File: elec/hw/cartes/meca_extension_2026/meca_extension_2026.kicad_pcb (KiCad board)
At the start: 2 copper layers, 126.2 x 84.5 mm, 177 parts, among them J1 2-1445051-3, J10 22053051, J11 B2B-XH-A, J12 22272021, J13 22053051, J14 22272031, J15 22272031, J16 5264-3P, J17 5267-3P, J18 5267-3P, J19 5267-3P, J2 B2B-XH-A, J20 5267-3P, J24 22053031, J25 22053031, J26 22053051, J27 22053041, J28 22053031, J29 22053031, J3 22272021, J4 22053051, J5 B2B-XH-A, J6 22272021, J7 22053051, J8 B2B-XH-A, J9 22272021, Q1 SI2310, Q10 SI2310, Q11 SI2310, Q12 2N7002, Q19 BSS84, Q2 SI2310, Q20 2N7002, Q3 2N7002, Q4 SI2310, Q5 SI2310, Q6 2N7002, Q7 SI2310, Q8 SI2310, Q9 2N7002, U1 TCA9548APWR, U11 LV14340DDAR, U2 PCA9535PW, U3 TLA2528IRTER, U4 TLV9061IDBVR, U5 TLV9061IDBVR, U6 TLV9061IDBVR, U7 TLV9061IDBVR, U8 74HCT238PW

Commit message: meca_extension : led added and J1 moved
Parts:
- moved J27 4.30 mm to (129.9, 52.4), turned to 60 degrees
- moved J26 2.82 mm to (121.5, 56.5), turned to 60 degrees
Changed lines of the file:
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@@
 		(tags "capacitor")
 		(property "Reference" "D9"
-			(at 66.5 7.07 180)
+			(at 0 1.75 180)
 			(layer "F.SilkS")
 			(effects
@@
 	(footprint "cocotter_connectors:22272041"
 		(layer "B.Cu")
-		(at 130.400148 56.635 -60)
+		(at 129.900148 52.365 60)
 		(property "Reference" "J27"
-			(at 0 6.35 120)
+			(at 0 6.35 240)
 			(unlocked yes)
 			(layer "B.SilkS")
@@
 		)
 		(property "Value" "22053041"
-			(at 0 -1.06 120)
+			(at 0 -1.06 240)
 			(unlocked yes)
 			(layer "B.Fab")
@@
 		)
 		(property "Datasheet" "https://www.molex.com/en-us/products/part-detail/22272041"
-			(at -0.000001 2.540001 120)
+			(at -0.000001 2.540001 240)
 			(unlocked yes)
 			(layer "B.Fab")
@@
 		)
 		(property "Description" "mini kk 4 voies vertical"
-			(at -0.000001 2.540001 120)
+			(at -0.000001 2.540001 240)
 			(unlocked yes)
 			(layer "B.Fab")
@@
 		)
 		(property "JLCPCB Part #" "C504991"
-			(at 0 0 300)
+			(at 0 0 60)
 			(unlocked yes)
 			(layer "B.Fab")
@@
 		(attr smd)
 		(fp_line
-			(start -2.899999 5.079999)
-			(end 2.9 5.08)
+			(start 2.899999 -5.079999)
+			(end -2.9 -5.08)
 			(stroke
 				(width 0.12)
@@
 		)
 		(fp_line
-			(start -2.9 3.81)
-			(end -2.9 -1.270001)
+			(start 2.899999 -5.079999)
+			(end 2.9 5.08)
 			(stroke
 				(width 0.12)
@@
 		)
 		(fp_line
-			(start -1.9 3.810001)
-			(end -1.9 -1.27)
+			(start -2.9 3.81)
+			(end -2.9 -1.270001)
 			(stroke
 				(width 0.12)
@@
 		)
 		(fp_line
-			(start 2.899999 -5.079999)
-			(end 2.9 5.08)
+			(start -1.9 3.810001)
+			(end -1.9 -1.27)
 			(stroke
 				(width 0.12)
@@
 		)
 		(fp_line
-			(start 2.899999 -5.079999)
-			(end -2.9 -5.08)
+			(start -2.899999 5.079999)
+			(end 2.9 5.08)
 			(stroke
 				(width 0.12)
@@
 		)
 		(fp_line
-			(start -2.899999 5.079999)
-			(end 2.9 5.08)
+			(start 2.899999 -5.079999)
+			(end -2.9 -5.08)
 			(stroke
 				(width 0.1)
@@
 		)
 		(fp_line
-			(start 2.9 5.08)
-			(end 2.899999 -5.079999)
+			(start -2.9 0)
+			(end -2.899999 5.079999)
 			(stroke
 				(width 0.1)
@@
 		)
 		(fp_line
-			(start -2.9 0)
-			(end -2.899999 5.079999)
+			(start -2.899999 5.079999)
+			(end 2.9 5.08)
 			(stroke
 				(width 0.1)
@@
 		)
 		(fp_line
-			(start 2.899999 -5.079999)
-			(end -2.9 -5.08)
+			(start 2.9 5.08)
+			(end 2.899999 -5.079999)
 			(stroke
 				(width 0.1)
@@
 		)
 		(fp_text user "${REFERENCE}"
-			(at 0 -1.23 120)
+			(at 0 -1.23 240)
 			(unlocked yes)
 			(layer "B.Fab")
@@
 		)
 		(pad "1" thru_hole rect
-			(at 0.000001 3.81 300)
+			(at 0.000001 3.81 60)
 			(size 2 2)
 			(drill 1.2)
@@
 		)
 		(pad "2" thru_hole oval
-			(at 0 1.27 300)
+			(at 0 1.27 60)
 			(size 2 2)
 			(drill 1.2)
@@
 		)
 		(pad "3" thru_hole oval
-			(at 0 -1.27 300)
+			(at 0 -1.27 60)
 			(size 2 2)
 			(drill 1.2)
@@
 		)
 		(pad "4" thru_hole oval
-			(at -0.000001 -3.81 300)
+			(at -0.000001 -3.81 60)
 			(size 2 2)
 			(drill 1.2)
@@
 	(footprint "cocotter_connectors:22272051"
 		(layer "B.Cu")
-		(at 120.800295 53.770001 120)
+		(at 121.5 56.5 60)
 		(property "Reference" "J26"
-			(at 0 7.62 300)
+			(at 0 7.62 240)
 			(unlocked yes)
 			(layer "B.SilkS")
@@
 		)
 		(property "Value" "22053051"
-			(at 0 -7.62 300)
+			(at 0 -7.62 240)
 			(unlocked yes)
 			(layer "B.Fab")
@@
 		)
 		(property "Datasheet" "https://www.molex.com/en-us/products/part-detail/22272051"
-			(at -0.000001 3.81 300)
+			(at -0.000001 3.81 240)
 			(unlocked yes)
 			(layer "B.Fab")
@@
 		)
 		(property "Description" "mini kk 5 voies vertical"
-			(at -0.000001 3.81 300)
+			(at -0.000001 3.81 240)
 			(unlocked yes)
 			(layer "B.Fab")
@@
 		)
 		(property "JLCPCB Part #" "C585785"
-			(at 0 0 120)
+			(at 0 0 60)
 			(unlocked yes)
 			(layer "B.Fab")
@@
 		)
 		(fp_line
-			(start -1.900001 3.81)
-			(end -1.9 -1.27)
+			(start -2.899999 3.81)
+			(end -2.9 -1.27)
 			(stroke
 				(width 0.12)
@@
 		)
 		(fp_line
-			(start -2.899999 3.81)
-			(end -2.9 -1.27)
+			(start -1.900001 3.81)
+			(end -1.9 -1.27)
 			(stroke
 				(width 0.12)
@@
 		(fp_poly
 			(pts
-				(xy -3.400001 6.81) (xy 3.400001 6.809999) (xy 3.400001 -6.81) (xy -3.400001 -6.809999)
+				(xy -3.400001 6.809999) (xy 3.400001 6.809999) (xy 3.400001 -6.809999) (xy -3.400001 -6.809999)
 			)
 			(stroke
@@
 		)
 		(fp_line
-			(start 2.9 6.35)
-			(end 2.900001 -6.35)
+			(start -2.900001 6.35)
+			(end 2.9 6.35)
 			(stroke
 				(width 0.1)
@@
 		)
 		(fp_line
-			(start -2.900001 6.35)
-			(end 2.9 6.35)
+			(start 2.9 6.35)
+			(end 2.900001 -6.35)
 			(stroke
 				(width 0.1)
@@
 		)
 		(fp_text user "${REFERENCE}"
-			(at 0 7.62 300)
+			(at 0 7.62 240)
 			(unlocked yes)
 			(layer "B.Fab")
@@
 		)
 		(pad "1" thru_hole rect
-			(at 0 5.08 120)
+			(at 0 5.08 60)
 			(size 2 2)
 			(drill 1.2)
@@
 		)
 		(pad "2" thru_hole oval
-			(at 0.000001 2.540001 120)
+			(at 0.000001 2.540001 60)
 			(size 2 2)
 			(drill 1.2)
@@
 		)
 		(pad "3" thru_hole oval
-			(at 0 0 120)
+			(at 0 0 60)
 			(size 2 2)
 			(drill 1.2)
@@
 		)
 		(pad "4" thru_hole oval
-			(at -0.000001 -2.540001 120)
+			(at -0.000001 -2.540001 60)
 			(size 2 2)
 			(drill 1.2)
@@
 		)
 		(pad "5" thru_hole oval
-			(at 0 -5.08 120)
+			(at 0 -5.08 60)
 			(size 2 2)
 			(drill 1.2)

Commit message: meca_ext: layout almost done
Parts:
- added R58: 2k2 1%, cocotter_resistor:r0603_reflow, B.Cu at (117.0, 88.5)
- added R59: 2k2 1%, cocotter_resistor:r0603_reflow, B.Cu at (115.0, 86.5)
- added R60: 2k2 1%, cocotter_resistor:r0603_reflow, B.Cu at (127.0, 87.3)
- added R61: 2k2 1%, cocotter_resistor:r0603_reflow, B.Cu at (127.0, 89.5)
- added TP5: TestPoint, cocotter_others:testpoint-THT-0.8mm, B.Cu at (119.5, 88.5)
- added TP6: TestPoint, cocotter_others:testpoint-THT-0.8mm, B.Cu at (117.5, 86.5)
- added TP7: TestPoint, cocotter_others:testpoint-THT-0.8mm, B.Cu at (123.5, 87.5)
- added TP8: TestPoint, cocotter_others:testpoint-THT-0.8mm, B.Cu at (123.5, 89.5)
- D9: moved to B.Cu
- moved R57 43.7 mm to (98.0, 81.3)
- moved D9 41.6 mm to (101.2, 81.3), turned to 180 degrees
- moved C1 16.3 mm to (131.0, 59.0), turned to -30 degrees
- moved R76 14.1 mm to (122.5, 62.5), turned to -30 degrees
- moved C12 9.82 mm to (177.0, 113.0), turned to 105 degrees
- moved R78 7.28 mm to (98.0, 95.0), turned to 180 degrees
- moved C21 6.04 mm to (100.0, 100.5), turned to 180 degrees
- moved C9 6.02 mm to (94.0, 76.0), turned to 180 degrees
- moved R77 5.70 mm to (101.0, 95.0), turned to 180 degrees
- moved R56 4.92 mm to (145.0, 86.0), turned to 90 degrees
- moved C13 4.03 mm to (100.0, 97.5), turned to 180 degrees
- moved C10 3.04 mm to (72.0, 98.5), turned to 180 degrees
- moved R79 1.76 mm to (97.0, 93.5), turned to 180 degrees
- moved C2 1.67 mm to (147.5, 96.8), turned to 90 degrees
- moved R46 1.41 mm to (95.5, 69.5), turned to 180 degrees
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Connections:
- J27 pad 1: /scl_3v3 -> GND
- J27 pad 2: /sda_3v3 -> /scl_3v3
- J27 pad 3: +3.3V -> /sda_3v3
- J27 pad 4: unconnected-(J27-Pad4) -> +3.3V
- U1 pad 13: /sda_4_3v3 -> Net-(U1-SD4)
- U1 pad 14: /scl_4_3v3 -> Net-(U1-SC4)
- U1 pad 15: /sda_5_3v3 -> Net-(U1-SD5)
- U1 pad 16: /scl_5_3v3 -> Net-(U1-SC5)
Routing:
- net +BATT: track 0.00 -> 300.8 mm
- net +5V: track 0.00 -> 222.8 mm, vias 0 -> 1
- net /digital_servo_cmd_3v3: track 0.00 -> 206.1 mm
- net /color_led_cmd_3v3: track 0.00 -> 197.9 mm, vias 0 -> 5
- net +3.3V: track 0.00 -> 197.9 mm, vias 0 -> 21
- net /scl_3v3: track 0.00 -> 154.4 mm, vias 0 -> 4
- net +6V: track 0.00 -> 153.8 mm, vias 0 -> 3
- net /sda_3v3: track 0.00 -> 152.7 mm, vias 0 -> 4
- net /pmp_cmd_0_3v3: track 0.00 -> 109.6 mm, vias 0 -> 2
- net /neopixel_cmd_3v3: track 0.00 -> 107.3 mm, vias 0 -> 1
- net /solenoid_valve_cmd_0_3v3: track 0.00 -> 93.1 mm, vias 0 -> 2
- net /neopixel_cmd_3_3v3: track 0.00 -> 84.4 mm, vias 0 -> 2
- net /pump_current_3_3v3: track 0.00 -> 83.2 mm, vias 0 -> 2
- net /pmp_cmd_1_3v3: track 0.00 -> 76.4 mm, vias 0 -> 4
- net /sda_2_3v3: track 0.00 -> 76.3 mm, vias 0 -> 2
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- added copper zone on In2.Cu, net +3.3V
- added copper zone on B.Cu, net +6V
- added copper zone on B.Cu, net GND
- added copper zone on F.Cu, net GND
- added copper zone on In1.Cu, net GND
- added copper zone on In2.Cu, net GND
- added copper zone on B.Cu, net Net-(C16-Pad1)
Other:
- copper layers 2 -> 4
- board text removed: "trous de fixation a replacer correctement, je les ai juste jetés"

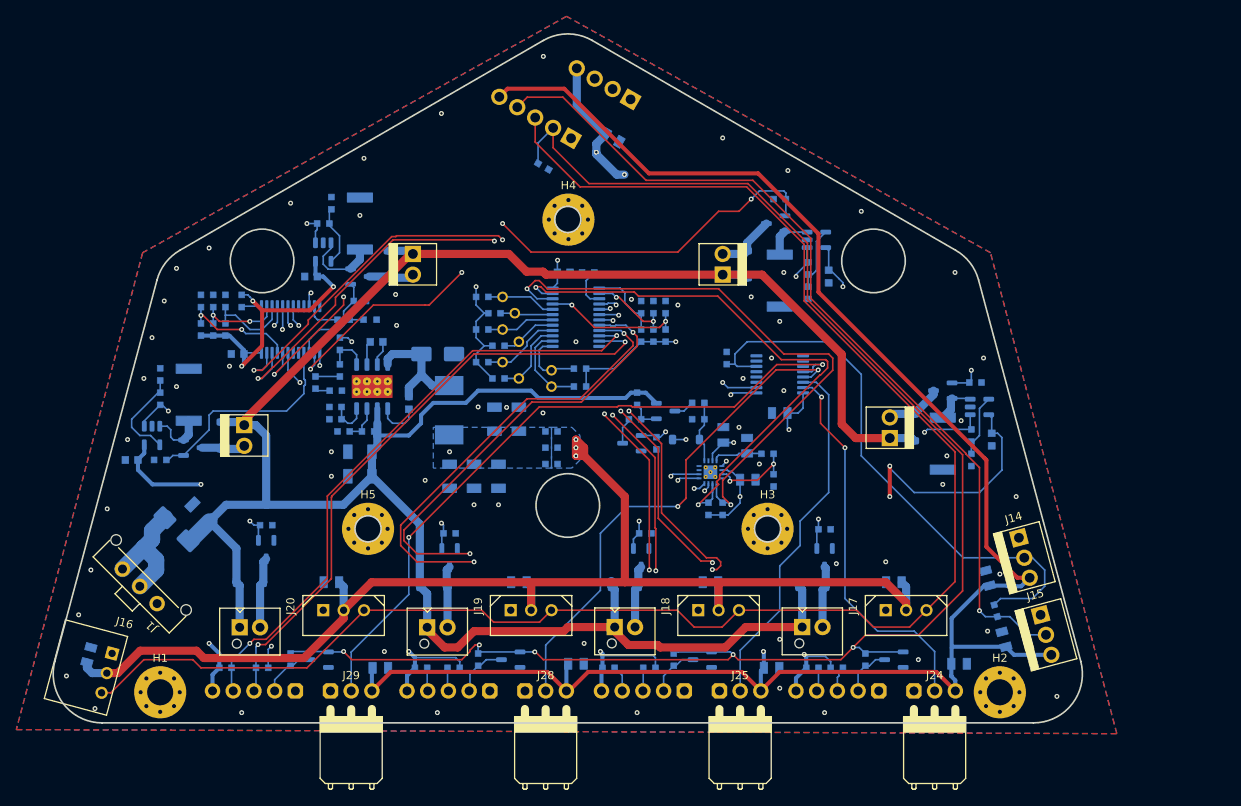
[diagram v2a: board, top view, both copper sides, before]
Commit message: meca ext : cleaning layout
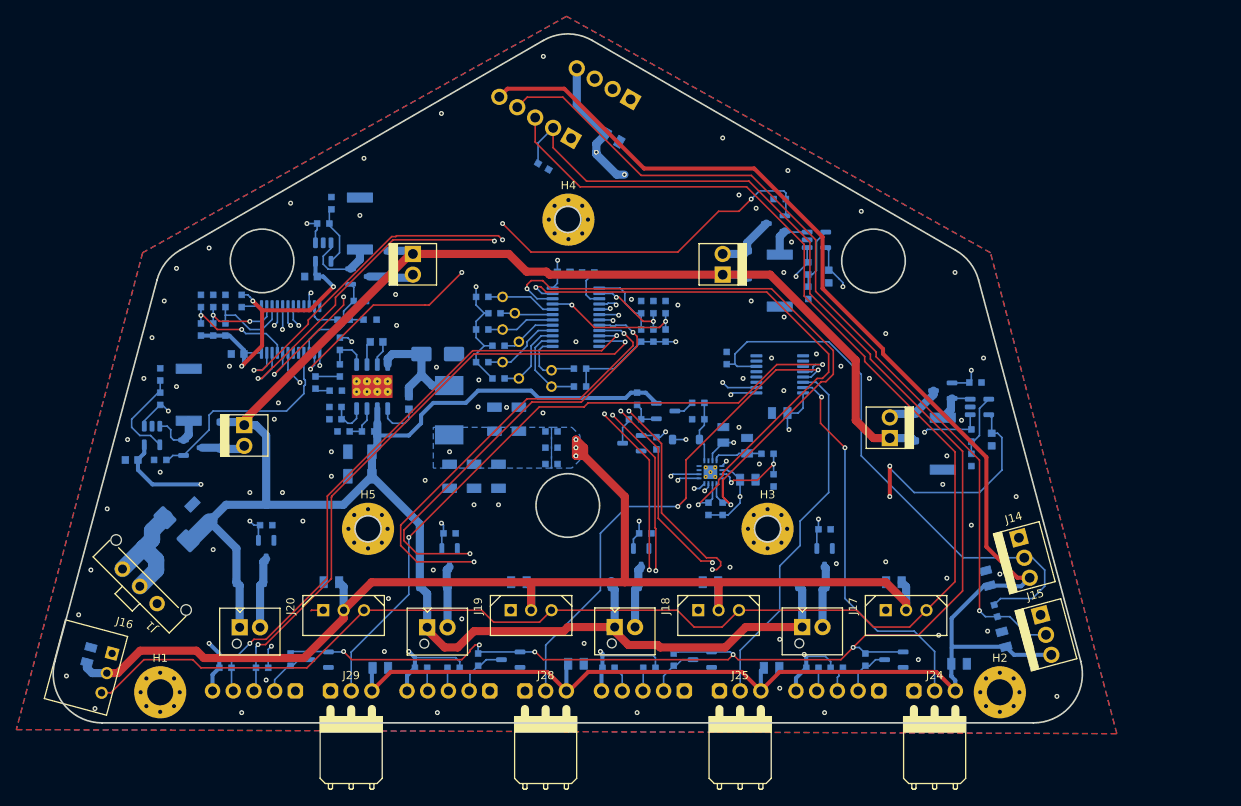
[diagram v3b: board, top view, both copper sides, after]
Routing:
- net /scl_3v3: track 154.4 -> 159.1 mm
- net +5V: track 222.8 -> 220.8 mm, vias 1 -> 0
- net GND: track 3.90 -> 5.43 mm, vias 64 -> 89
- net /solenoid_valve_cmd_0_3v3: track 93.1 -> 94.4 mm
- net +BATT: track 300.8 -> 300.1 mm
- net /pump_current_2_3v3: track 72.6 -> 72.1 mm

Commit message: meca_extension routing review and schematic correction
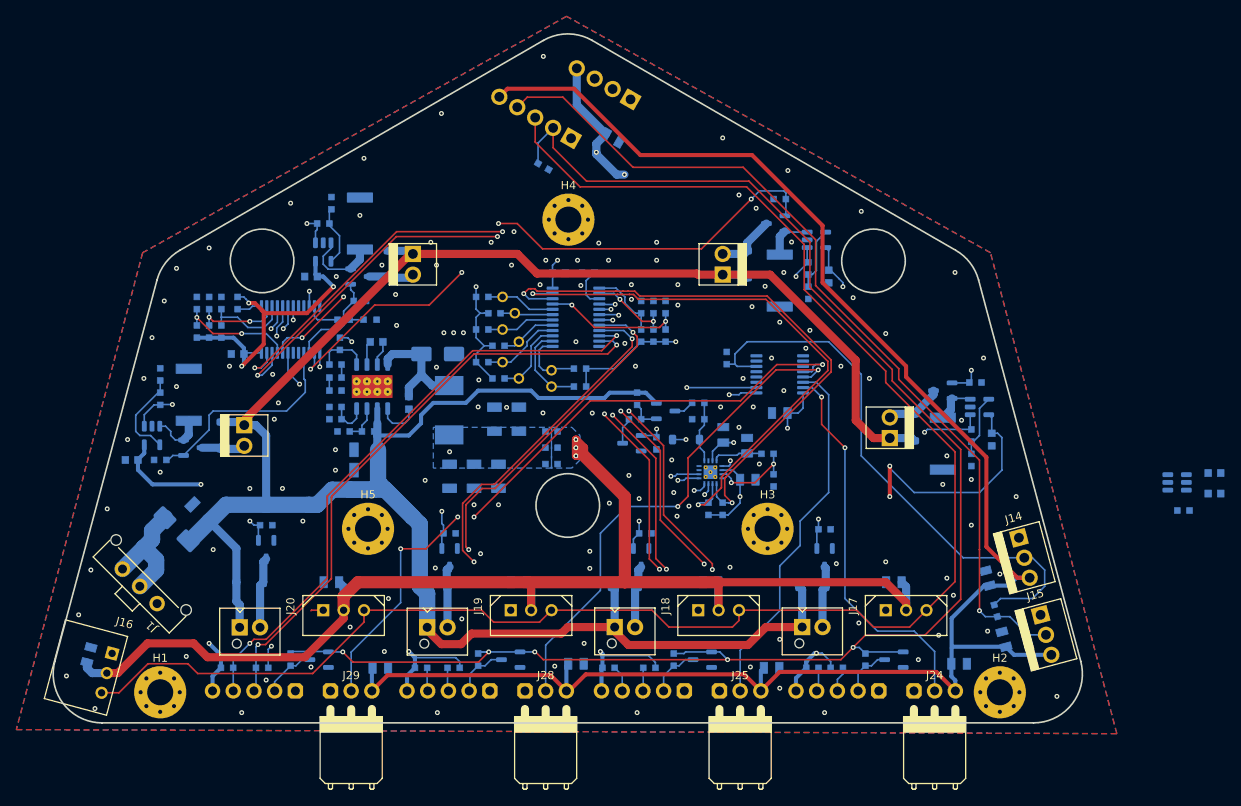
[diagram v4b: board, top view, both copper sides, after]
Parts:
- added C33: 100nF 50V, cocotter_capacitors:C_0603_1608Metric, B.Cu at (204.8, 100.1)
- added C34: 100nF 50V, cocotter_capacitors:C_0603_1608Metric, B.Cu at (204.8, 102.6)
- added R62: 100k, cocotter_resistor:r0603_reflow, B.Cu at (201.0, 104.7)
- added U9: SN74LVC1T45DBV, Package_TO_SOT_SMD:SOT-23-6, B.Cu at (200.2, 101.3)
- moved R86 2.53 mm to (97.0, 88.4), turned to 0 degrees
- moved C21 1.06 mm to (100.8, 99.8)
- moved R87 0.90 mm to (97.0, 86.8), turned to 0 degrees
- moved C13 0.79 mm to (100.8, 97.2)
- moved C5 0.61 mm to (124.4, 75.6)
- moved R10 0.56 mm to (81.5, 79.2)
- moved R12 0.56 mm to (85.0, 79.2)
- moved R15 0.56 mm to (83.0, 82.8)
- moved R16 0.56 mm to (83.0, 79.2)
- moved R4 0.56 mm to (80.0, 82.8)
- moved R5 0.56 mm to (80.0, 79.2)
- moved R9 0.56 mm to (81.5, 82.8)
- moved R50 0.20 mm to (83.7, 124.0)
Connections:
- J14 pad 2: /neopixel_ret_3v3 -> /neopixel_cmd_5v
- J15 pad 2: /neopixel_cmd_3v3 -> /neopixel_cmd_5v
- R55 pad 1: /neopixel_cmd_3v3 -> /neopixel_cmd_5v
- R55 pad 2: /neopixel_ret_3v3 -> /neopixel_cmd_5v
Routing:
- net /scl_2_3v3: track 75.1 -> 61.9 mm
- net /sda_2_3v3: track 76.3 -> 63.4 mm
- net +BATT: track 300.1 -> 309.1 mm
- net /<NO NET>: track 75.2 -> 69.7 mm
- net /scl_3v3: track 159.1 -> 154.3 mm
- net /solenoid_valve_cmd_3_3v3: track 36.0 -> 33.5 mm
- net /sda_0_3v3: track 67.3 -> 65.2 mm
- net /scl_3_3v3: track 75.5 -> 73.3 mm
- net /digital_servo_cmd_3v3: track 206.1 -> 207.8 mm
- net +6V: track 153.8 -> 155.4 mm
- net Net-(R86-Pad2): track 3.00 -> 1.60 mm
- net /solenoid_valve_cmd_2_3v3: track 39.1 -> 40.4 mm
- net /pump_current_2_3v3: track 72.1 -> 70.9 mm
- net /enable_vbatt_meas_3v3: track 55.6 -> 54.4 mm
- net /fb_5v: track 5.25 -> 6.44 mm
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- added copper zone on In2.Cu, net +6V
- removed copper zone on In2.Cu, net GND
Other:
- outline, holes or cut-outs redrawn
